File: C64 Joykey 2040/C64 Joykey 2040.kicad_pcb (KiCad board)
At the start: 2 copper layers, 99.7 x 74.9 mm, 69 parts, among them J1 Port_1, J2 Port_2, J4 Expansion, M1 Mounting, M2 Mounting, M3 Mounting, M4 Mounting, Q1 2N3904, SW1 UP, SW10 P1_FIRE2, SW11 P2_FIRE3, SW12 P1_FIRE5, SW13 P1_FIRE6, SW2 DOWN, SW3 LEFT, SW4 RIGHT, SW5 P1_FIRE4, SW6 P2_FIRE1, SW7 P1_FIRE1, SW8 P1_FIRE3, SW9 P2_FIRE2, U1 RP2040-Zero

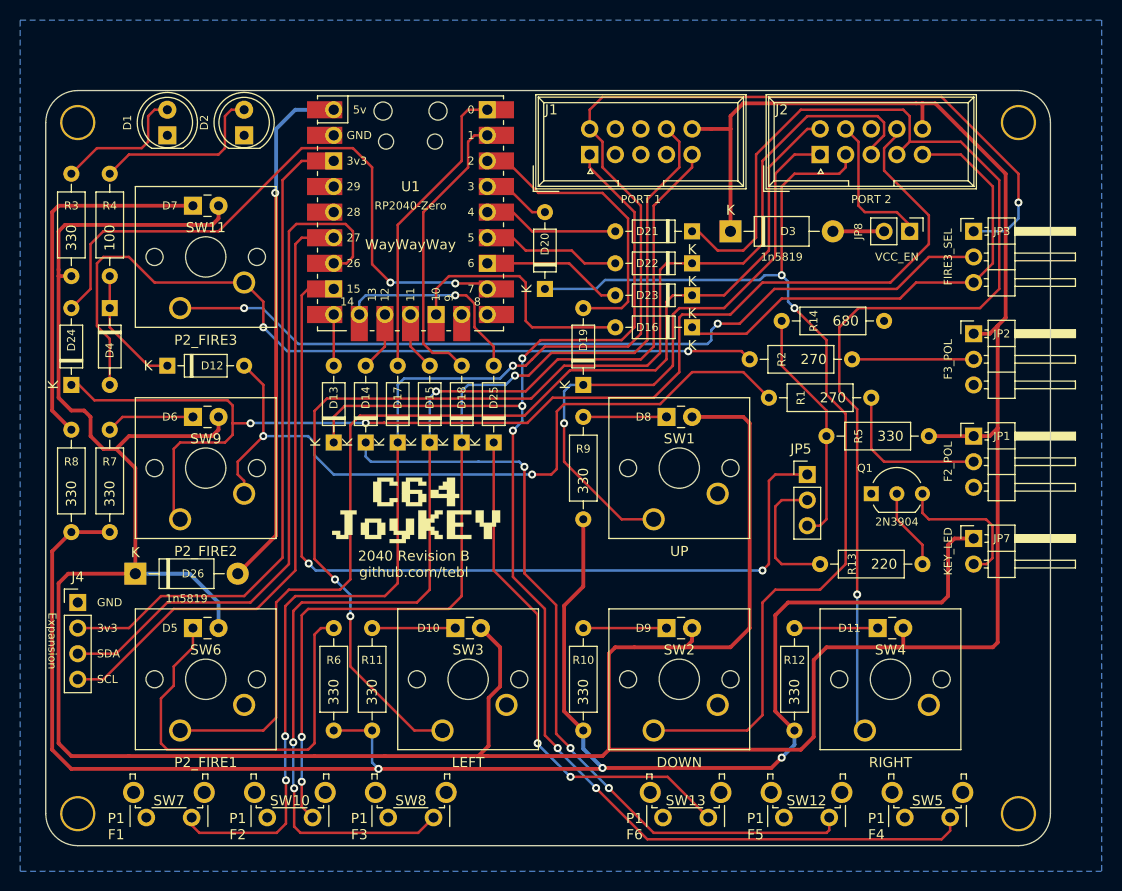
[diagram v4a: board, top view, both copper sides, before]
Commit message: Build tweaks to include LED labels
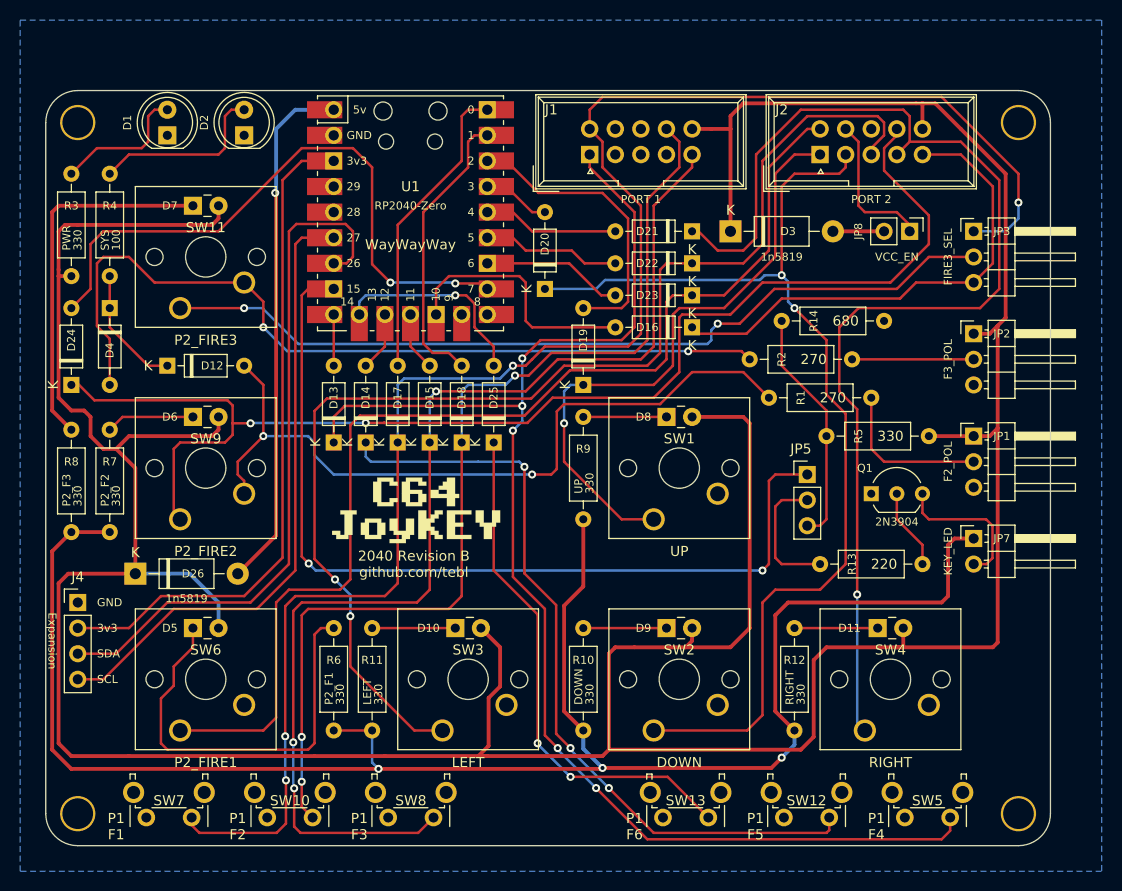
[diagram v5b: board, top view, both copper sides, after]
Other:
- board text added: "DOWN"
- board text added: "LEFT"
- board text added: "P2_F1"
- board text added: "P2_F2"
- board text added: "P2_F3"
- board text added: "PWR"
- board text added: "RIGHT"
- board text added: "SYS"
- board text added: "UP"
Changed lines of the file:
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@@
 		)
 		(property "Value" "330"
-			(at 6.35 0 90)
+			(at 7.62 -0.635 90)
 			(layer "F.SilkS")
 			(effects
 				(font
-					(size 1 1)
-					(thickness 0.15)
+					(size 0.8 0.8)
+					(thickness 0.1)
 				)
+				(justify left)
 			)
 		)
@@
 		)
 		(property "Value" "100"
-			(at 6.35 0 90)
+			(at 7.62 -0.635 90)
 			(layer "F.SilkS")
 			(effects
 				(font
-					(size 1 1)
-					(thickness 0.15)
+					(size 0.8 0.8)
+					(thickness 0.1)
 				)
+				(justify left)
 			)
 		)
@@
 		)
 		(property "Value" "330"
-			(at 6.35 0 90)
+			(at 7.62 -0.635 90)
 			(layer "F.SilkS")
 			(effects
 				(font
-					(size 1 1)
-					(thickness 0.15)
+					(size 0.8 0.8)
+					(thickness 0.1)
 				)
+				(justify left)
 			)
 		)
@@
 		)
 		(property "Value" "330"
-			(at 6.35 0 90)
+			(at 7.62 -0.635 90)
 			(layer "F.SilkS")
 			(effects
 				(font
-					(size 1 1)
-					(thickness 0.15)
+					(size 0.8 0.8)
+					(thickness 0.1)
 				)
+				(justify left)
 			)
 		)
@@
 		)
 		(property "Value" "330"
-			(at 6.35 0 90)
+			(at 7.62 -0.635 90)
 			(layer "F.SilkS")
 			(effects
 				(font
-					(size 1 1)
-					(thickness 0.15)
+					(size 0.8 0.8)
+					(thickness 0.1)
 				)
+				(justify left)
 			)
 		)
@@
 		)
 		(property "Value" "330"
-			(at 6.35 0 90)
+			(at 7.62 -0.635 90)
 			(layer "F.SilkS")
 			(effects
 				(font
-					(size 1 1)
-					(thickness 0.15)
+					(size 0.8 0.8)
+					(thickness 0.1)
 				)
+				(justify left)
 			)
 		)
@@
 		)
 		(property "Value" "330"
-			(at 6.35 0 90)
+			(at 7.62 -0.635 90)
 			(layer "F.SilkS")
 			(effects
 				(font
-					(size 1 1)
-					(thickness 0.15)
+					(size 0.8 0.8)
+					(thickness 0.1)
 				)
+				(justify left)
 			)
 		)
@@
 		)
 		(property "Value" "330"
-			(at 6.35 0 90)
+			(at 7.62 -0.635 90)
 			(layer "F.SilkS")
 			(effects
 				(font
-					(size 1 1)
-					(thickness 0.15)
+					(size 0.8 0.8)
+					(thickness 0.1)
 				)
+				(justify left)
 			)
 		)
@@
 		)
 		(property "Value" "330"
-			(at 6.35 0 90)
+			(at 7.62 -0.635 90)
 			(layer "F.SilkS")
 			(effects
 				(font
-					(size 1 1)
-					(thickness 0.15)
+					(size 0.8 0.8)
+					(thickness 0.1)
 				)
+				(justify left)
 			)
 		)
@@
 			)
 		)
-		(fp_text user "Copper Keepouts shown on Dwgs layer"
-			(at 0.1 -30.2 0)
-			(layer "Cmts.User")
-			(effects
-				(font
-					(size 1 1)
-					(thickness 0.15)
-				)
-			)
-		)
 		(fp_text user "${REFERENCE}"
 			(at 0 0 180)
@@
 		)
 		(fp_text user "${REFERENCE}"
-			(at 5.08 0 360)
+			(at 5.08 0 0)
 			(layer "F.Fab")
 			(effects
@@
 		)
 		(property "Value" "Expansion"
-			(at -2.54 3.81 270)
+			(at -2.54 3.81 -90)
 			(unlocked yes)
 			(layer "F.SilkS")
@@
 		)
 	)
+	(gr_text "DOWN"
+		(at 194.31 143.51 90)
+		(layer "F.SilkS")
+		(effects
+			(font
+				(size 0.8 0.8)
+				(thickness 0.1)
+			)
+			(justify left bottom)
+		)
+	)
 	(gr_text "P1\nF1"
 		(at 147.955 155.575 0)
@@
 		)
 	)
+	(gr_text "RIGHT"
+		(at 215.265 143.51 90)
+		(layer "F.SilkS")
+		(effects
+			(font
+				(size 0.8 0.8)
+				(thickness 0.1)
+			)
+			(justify left bottom)
+		)
+	)
 	(gr_text "P1\nF5"
 		(at 211.393 155.575 0)
@@
 		)
 	)
+	(gr_text "UP"
+		(at 194.31 122.555 90)
+		(layer "F.SilkS")
+		(effects
+			(font
+				(size 0.8 0.8)
+				(thickness 0.1)
+			)
+			(justify left bottom)
+		)
+	)
 	(gr_text "SDA"
 		(at 146.05 138.43 0)
@@
 		)
 	)
+	(gr_text "PWR"
+		(at 143.51 98.425 90)
+		(layer "F.SilkS")
+		(effects
+			(font
+				(size 0.8 0.8)
+				(thickness 0.1)
+			)
+			(justify left bottom)
+		)
+	)
+	(gr_text "P2_F3"
+		(at 143.51 123.825 90)
+		(layer "F.SilkS")
+		(effects
+			(font
+				(size 0.8 0.8)
+				(thickness 0.1)
+			)
+			(justify left bottom)
+		)
+	)
+	(gr_text "SYS"
+		(at 147.32 98.425 90)
+		(layer "F.SilkS")
+		(effects
+			(font
+				(size 0.8 0.8)
+				(thickness 0.1)
+			)
+			(justify left bottom)
+		)
+	)
 	(gr_text "GND"
 		(at 146.05 133.35 0)
@@
 		)
 	)
+	(gr_text "P2_F2"
+		(at 147.32 123.825 90)
+		(layer "F.SilkS")
+		(effects
+			(font
+				(size 0.8 0.8)
+				(thickness 0.1)
+			)
+			(justify left bottom)
+		)
+	)
+	(gr_text "LEFT"
+		(at 173.355 143.51 90)
+		(layer "F.SilkS")
+		(effects
+			(font
+				(size 0.8 0.8)
+				(thickness 0.1)
+			)
+			(justify left bottom)
+		)
+	)
 	(gr_text "SCL"
 		(at 146.05 140.97 0)
@@
 		)
 	)
+	(gr_text "P2_F1"
+		(at 169.545 143.51 90)
+		(layer "F.SilkS")
+		(effects
+			(font
+				(size 0.8 0.8)
+				(thickness 0.1)
+			)
+			(justify left bottom)
+		)
+	)

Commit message: Slight build tweaks for clarity
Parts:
- U1: footprint pi_pico:RP2040-Zero -> pi_pico:RP2040-Zero-THT
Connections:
- net /L2_1 renamed /L2
- net /R2_1 renamed /R2
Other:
- board text added: "Always configure FIRE2/FIRE3 polarity according to what's required by the system. Leave unjumpered (N/C) if you are not sure."
- board text added: "IMPORTANT!"
- board text added: "You break it, you fix it!"
- board text removed: "IMPORTANT! Always configure FIRE2/FIRE3 polarity according to what's required by the system. Leave unjumpered (N/C) if you are not sure. You break it, you fix it!"

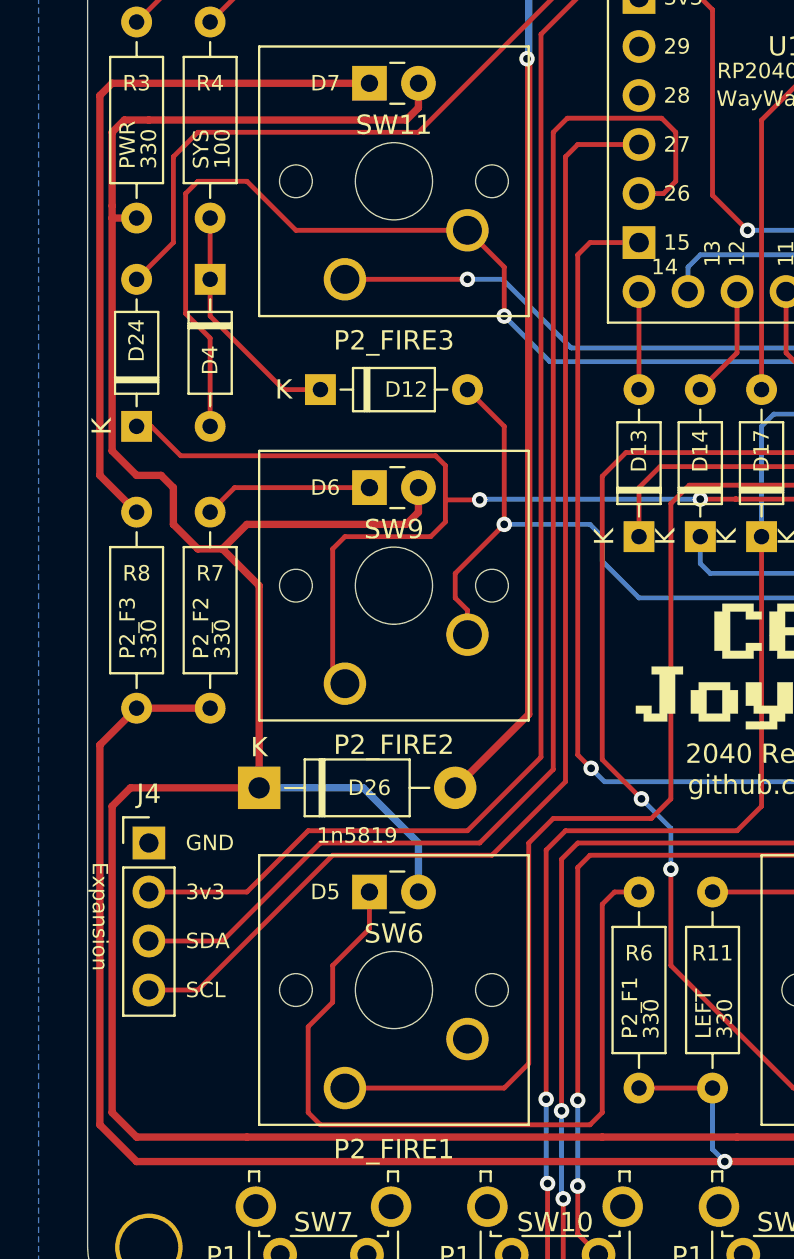
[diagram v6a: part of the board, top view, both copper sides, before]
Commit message: Change expansion header to JST XH, but in a right-angle variant
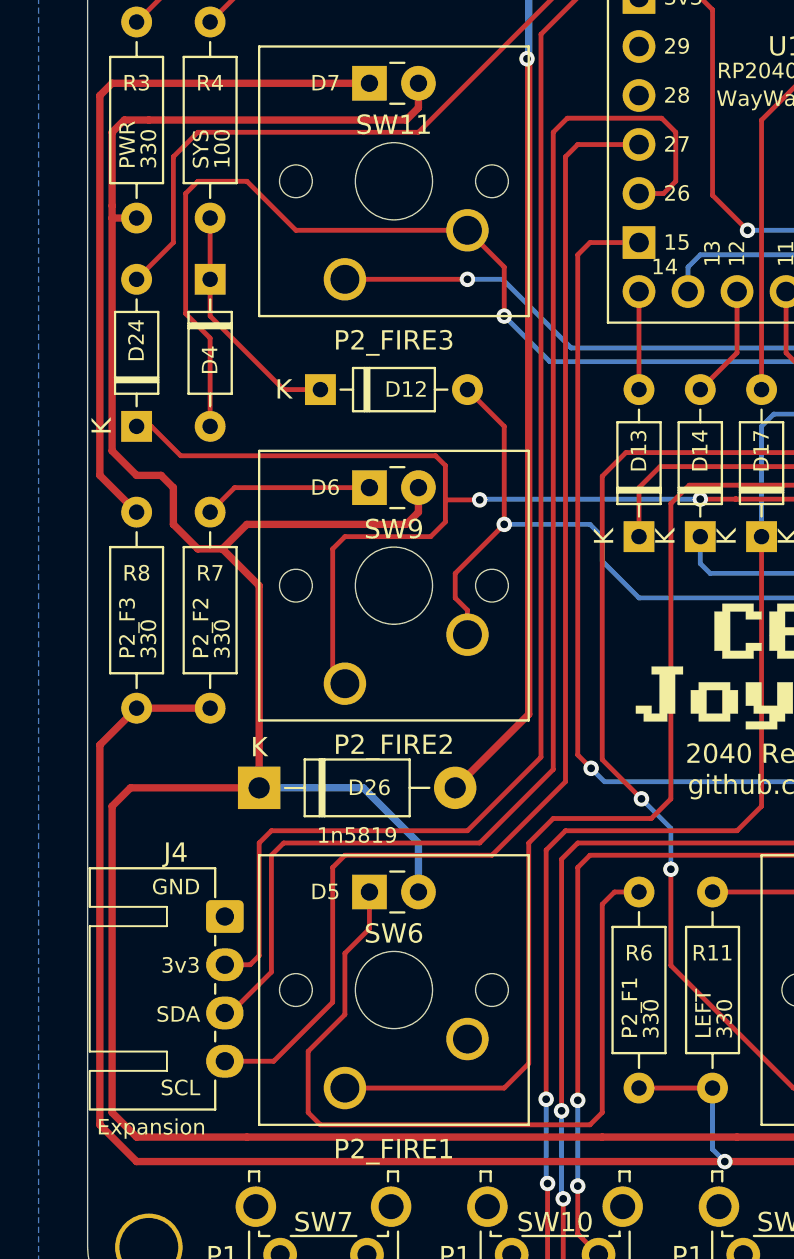
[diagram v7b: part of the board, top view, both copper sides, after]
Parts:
- J4: footprint Connector_PinHeader_2.54mm:PinHeader_1x04_P2.54mm_Vertical -> JST_XH_Right_Angle:JST_XH_B4B-XH-A_1x04_P2.50mm_Right_Angle
- moved J4 5.48 mm to (148.1, 137.2)
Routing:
- net I2C_SCL: track 62.5 -> 64.2 mm
- net I2C_SDA: track 69.3 -> 70.5 mm
- net +3V3: track 66.5 -> 67.6 mm
